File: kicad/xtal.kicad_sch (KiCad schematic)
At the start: 12 parts, among them Q1 NMOS, Q11 PMOS, Q12 NMOS, Q4 NMOS, Q6 PMOS, Y2 Crystal

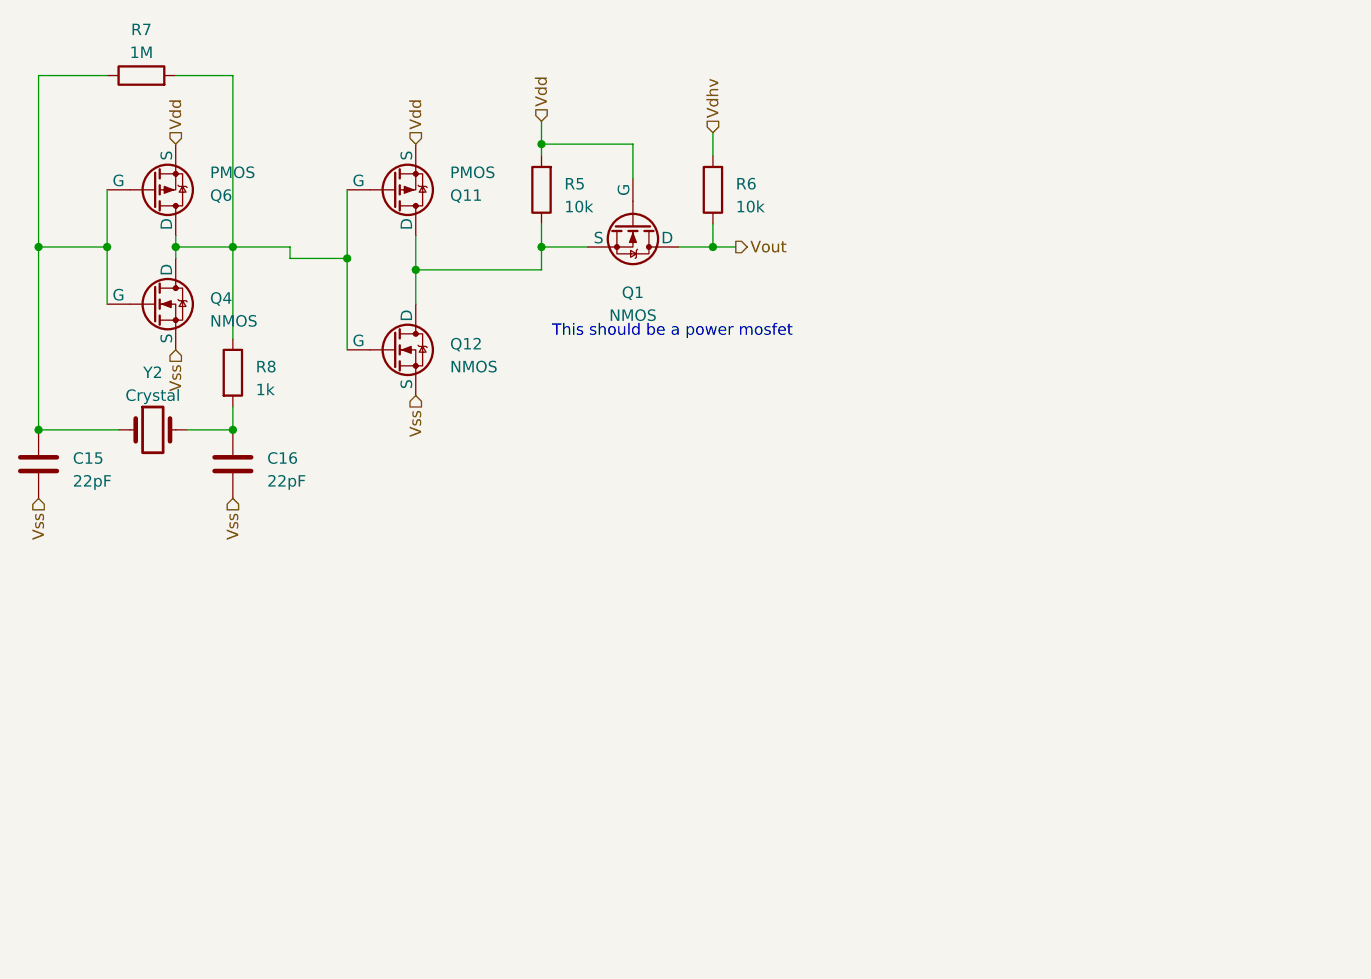
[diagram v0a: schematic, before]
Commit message: Add inverter driver
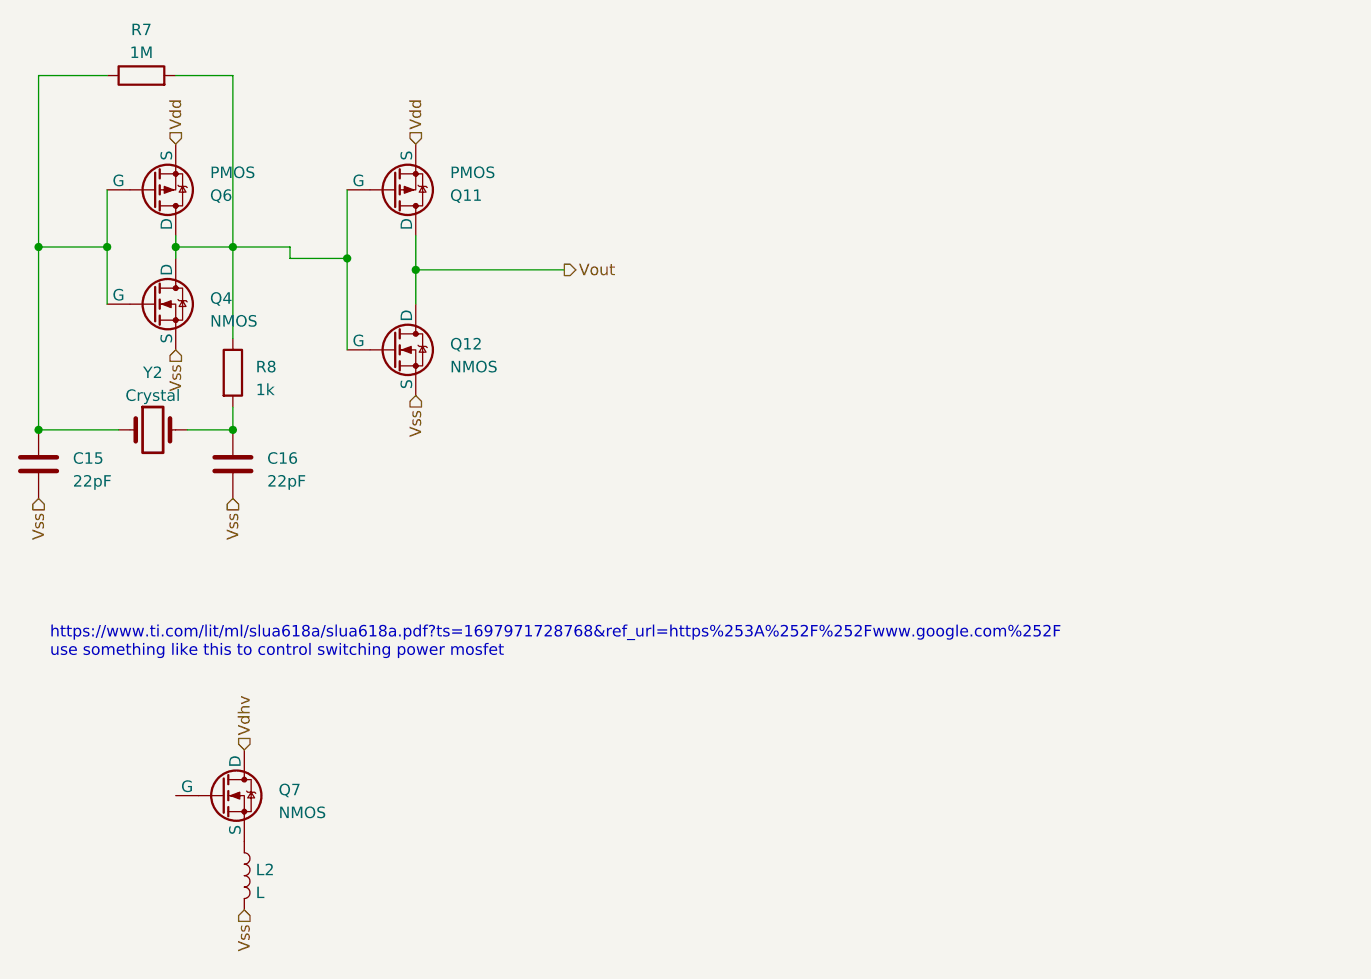
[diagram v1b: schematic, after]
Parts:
- removed Q1: NMOS, symbol Simulation_SPICE:NMOS
- removed R5, R6: 10k, symbol Device:R
- added L2: L, symbol Device:L
- added Q7: NMOS, symbol Simulation_SPICE:NMOS
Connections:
- net Vdhv: now also Q7.1 (D)
- net Vout: now also Q11.1 (D), Q12.1 (D)
- net Vss: now also L2.2
- new net: L2.1, Q7.3 (S)
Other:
- note added: "https://www.ti.com/lit/ml/slua618a/slua618a.pdf?ts=1697971728768&ref_url=https%253A%252F%252Fwww.google.com%252F use something like this to control switching power mosfet"
- note removed: "This should be a power mosfet"
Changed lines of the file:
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@@
   (junction (at 86.36 99.06) (diameter 0) (color 0 0 0 0)
   )
-  (junction (at 142.24 78.74) (diameter 0) (color 0 0 0 0)
-  )
   (junction (at 101.6 78.74) (diameter 0) (color 0 0 0 0)
   )
-  (junction (at 161.29 78.74) (diameter 0) (color 0 0 0 0)
-  )
   (junction (at 107.95 78.74) (diameter 0) (color 0 0 0 0)
   )
@@
   (junction (at 107.95 99.06) (diameter 0) (color 0 0 0 0)
   )
-  (junction (at 142.24 67.31) (diameter 0) (color 0 0 0 0)
-  )
   (junction (at 93.98 78.74) (diameter 0) (color 0 0 0 0)
   )
@@
     (stroke (width 0) (type default))
   )
-  (wire (pts (xy 161.29 66.04) (xy 161.29 68.58))
-    (stroke (width 0) (type default))
-  )
   (wire (pts (xy 93.98 78.74) (xy 93.98 85.09))
     (stroke (width 0) (type default))
@@
     (stroke (width 0) (type default))
   )
-  (wire (pts (xy 142.24 81.28) (xy 142.24 78.74))
-    (stroke (width 0) (type default))
-  )
-  (wire (pts (xy 128.27 81.28) (xy 142.24 81.28))
-    (stroke (width 0) (type default))
-  )
-  (wire (pts (xy 142.24 67.31) (xy 142.24 68.58))
-    (stroke (width 0) (type default))
-  )
   (wire (pts (xy 93.98 72.39) (xy 93.98 78.74))
     (stroke (width 0) (type default))
   )
-  (wire (pts (xy 161.29 78.74) (xy 163.83 78.74))
-    (stroke (width 0) (type default))
-  )
-  (wire (pts (xy 142.24 78.74) (xy 147.32 78.74))
+  (wire (pts (xy 128.27 81.28) (xy 144.78 81.28))
     (stroke (width 0) (type default))
   )
@@
     (stroke (width 0) (type default))
   )
-  (wire (pts (xy 152.4 71.12) (xy 152.4 67.31))
-    (stroke (width 0) (type default))
-  )
   (wire (pts (xy 120.65 80.01) (xy 120.65 90.17))
     (stroke (width 0) (type default))
@@
     (stroke (width 0) (type default))
   )
-  (wire (pts (xy 142.24 64.77) (xy 142.24 67.31))
-    (stroke (width 0) (type default))
-  )
   (wire (pts (xy 93.98 59.69) (xy 86.36 59.69))
     (stroke (width 0) (type default))
@@
     (stroke (width 0) (type default))
   )
-  (wire (pts (xy 152.4 67.31) (xy 142.24 67.31))
-    (stroke (width 0) (type default))
-  )
   (wire (pts (xy 107.95 88.9) (xy 107.95 78.74))
     (stroke (width 0) (type default))
   )
-  (wire (pts (xy 157.48 78.74) (xy 161.29 78.74))
-    (stroke (width 0) (type default))
-  )
   (wire (pts (xy 86.36 99.06) (xy 95.25 99.06))
     (stroke (width 0) (type default))
   )
-  (wire (pts (xy 142.24 76.2) (xy 142.24 78.74))
-    (stroke (width 0) (type default))
-  )
-  (wire (pts (xy 161.29 78.74) (xy 161.29 76.2))
-    (stroke (width 0) (type default))
-  )
   (wire (pts (xy 86.36 78.74) (xy 86.36 99.06))
     (stroke (width 0) (type default))
@@
     (stroke (width 0) (type default))
   )
-  (text "This should be a power mosfet" (at 170.18 88.9 0)
-    (effects (font (size 1.27 1.27)) (justify right bottom))
-  )
-  (hierarchical_label "Vdd" (shape input) (at 142.24 64.77 90) (fields_autoplaced)
-    (effects (font (size 1.27 1.27)) (justify left))
+  (text "https://www.ti.com/lit/ml/slua618a/slua618a.pdf?ts=1697971728768&ref_url=https%253A%252F%252Fwww.google.com%252F\nuse something like this to control switching power mosfet"
+    (at 87.63 124.46 0)
+    (effects (font (size 1.27 1.27)) (justify left bottom))
   )
   (hierarchical_label "Vss" (shape input) (at 107.95 106.68 270) (fields_autoplaced)
@@
     (effects (font (size 1.27 1.27)) (justify left))
   )
+  (hierarchical_label "Vss" (shape input) (at 109.22 152.4 270) (fields_autoplaced)
+    (effects (font (size 1.27 1.27)) (justify right))
+  )
   (hierarchical_label "Vss" (shape input) (at 128.27 95.25 270) (fields_autoplaced)
     (effects (font (size 1.27 1.27)) (justify right))
@@
     (effects (font (size 1.27 1.27)) (justify left))
   )
+  (hierarchical_label "Vdhv" (shape input) (at 109.22 134.62 90) (fields_autoplaced)
+    (effects (font (size 1.27 1.27)) (justify left))
+  )
   (hierarchical_label "Vss" (shape input) (at 101.6 90.17 270) (fields_autoplaced)
     (effects (font (size 1.27 1.27)) (justify right))
   )
-  (hierarchical_label "Vout" (shape output) (at 163.83 78.74 0) (fields_autoplaced)
-    (effects (font (size 1.27 1.27)) (justify left))
-  )
-  (hierarchical_label "Vdhv" (shape input) (at 161.29 66.04 90) (fields_autoplaced)
+  (hierarchical_label "Vout" (shape output) (at 144.78 81.28 0) (fields_autoplaced)
     (effects (font (size 1.27 1.27)) (justify left))
   )
@@
     )
   )
-  (symbol (lib_id "Device:R") (at 161.29 72.39 180) (unit 1)
-    (in_bom yes) (on_board yes) (dnp no) (fields_autoplaced)
-    (property "Reference" "R6" (at 163.83 71.755 0)
-      (effects (font (size 1.27 1.27)) (justify right))
-    )
-    (property "Value" "10k" (at 163.83 74.295 0)
-      (effects (font (size 1.27 1.27)) (justify right))
-    )
-    (property "Footprint" "" (at 163.068 72.39 90)
-      (effects (font (size 1.27 1.27)) hide)
-    )
-    (property "Datasheet" "~" (at 161.29 72.39 0)
-      (effects (font (size 1.27 1.27)) hide)
-    )
-    (pin "1")
-    (pin "2")
-    (instances
-      (project "kicad"
-        (path "/85f8f747-8376-4af6-9da4-afbb0f4bcd36/c5aef724-8676-4c81-889e-041c5ca81271/e305aaec-b373-422a-b2cb-386e797e1bef"
-          (reference "R6") (unit 1)
+  (symbol (lib_id "Device:L") (at 109.22 148.59 0) (unit 1)
+    (in_bom yes) (on_board yes) (dnp no) (fields_autoplaced)
+    (property "Reference" "L2" (at 110.49 147.955 0)
+      (effects (font (size 1.27 1.27)) (justify left))
+    )
+    (property "Value" "L" (at 110.49 150.495 0)
+      (effects (font (size 1.27 1.27)) (justify left))
+    )
+    (property "Footprint" "" (at 109.22 148.59 0)
+      (effects (font (size 1.27 1.27)) hide)
+    )
+    (property "Datasheet" "~" (at 109.22 148.59 0)
+      (effects (font (size 1.27 1.27)) hide)
+    )
+    (pin "1")
+    (pin "2")
+    (instances
+      (project "kicad"
+        (path "/85f8f747-8376-4af6-9da4-afbb0f4bcd36/c5aef724-8676-4c81-889e-041c5ca81271/e305aaec-b373-422a-b2cb-386e797e1bef"
+          (reference "L2") (unit 1)
         )
       )
@@
     )
   )
-  (symbol (lib_id "Simulation_SPICE:NMOS") (at 152.4 76.2 270) (unit 1)
-    (in_bom yes) (on_board yes) (dnp no) (fields_autoplaced)
-    (property "Reference" "Q1" (at 152.4 83.82 90)
-      (effects (font (size 1.27 1.27)))
-    )
-    (property "Value" "NMOS" (at 152.4 86.36 90)
-      (effects (font (size 1.27 1.27)))
-    )
-    (property "Footprint" "" (at 154.94 81.28 0)
-      (effects (font (size 1.27 1.27)) hide)
-    )
-    (property "Datasheet" "https://ngspice.sourceforge.io/docs/ngspice-manual.pdf" (at 139.7 76.2 0)
-      (effects (font (size 1.27 1.27)) hide)
-    )
-    (property "Sim.Device" "NMOS" (at 135.255 76.2 0)
-      (effects (font (size 1.27 1.27)) hide)
-    )
-    (property "Sim.Type" "VDMOS" (at 133.35 76.2 0)
-      (effects (font (size 1.27 1.27)) hide)
-    )
-    (property "Sim.Pins" "1=D 2=G 3=S" (at 137.16 76.2 0)
-      (effects (font (size 1.27 1.27)) hide)
-    )
-    (pin "1")
-    (pin "2")
-    (pin "3")
-    (instances
-      (project "kicad"
-        (path "/85f8f747-8376-4af6-9da4-afbb0f4bcd36/c5aef724-8676-4c81-889e-041c5ca81271/e305aaec-b373-422a-b2cb-386e797e1bef"
-          (reference "Q1") (unit 1)
-        )
-      )
-    )
-  )
   (symbol (lib_id "Device:Crystal") (at 99.06 99.06 0) (unit 1)
     (in_bom yes) (on_board yes) (dnp no) (fields_autoplaced)
@@
     )
   )
+  (symbol (lib_id "Simulation_SPICE:NMOS") (at 106.68 139.7 0) (unit 1)
+    (in_bom yes) (on_board yes) (dnp no) (fields_autoplaced)
+    (property "Reference" "Q7" (at 113.03 139.065 0)
+      (effects (font (size 1.27 1.27)) (justify left))
+    )
+    (property "Value" "NMOS" (at 113.03 141.605 0)
+      (effects (font (size 1.27 1.27)) (justify left))
+    )
+    (property "Footprint" "" (at 111.76 137.16 0)
+      (effects (font (size 1.27 1.27)) hide)
+    )
+    (property "Datasheet" "https://ngspice.sourceforge.io/docs/ngspice-manual.pdf" (at 106.68 152.4 0)
+      (effects (font (size 1.27 1.27)) hide)
+    )
+    (property "Sim.Device" "NMOS" (at 106.68 156.845 0)
+      (effects (font (size 1.27 1.27)) hide)
+    )
+    (property "Sim.Type" "VDMOS" (at 106.68 158.75 0)
+      (effects (font (size 1.27 1.27)) hide)
+    )
+    (property "Sim.Pins" "1=D 2=G 3=S" (at 106.68 154.94 0)
+      (effects (font (size 1.27 1.27)) hide)
+    )
+    (pin "1")
+    (pin "2")
+    (pin "3")
+    (instances
+      (project "kicad"
+        (path "/85f8f747-8376-4af6-9da4-afbb0f4bcd36/c5aef724-8676-4c81-889e-041c5ca81271/e305aaec-b373-422a-b2cb-386e797e1bef"
+          (reference "Q7") (unit 1)
+        )
+      )
+    )
+  )
   (symbol (lib_id "Simulation_SPICE:NMOS") (at 125.73 90.17 0) (unit 1)
     (in_bom yes) (on_board yes) (dnp no) (fields_autoplaced)
@@
         )
       )
-    )
-  )
-  (symbol (lib_id "Device:R") (at 142.24 72.39 180) (unit 1)
-    (in_bom yes) (on_board yes) (dnp no) (fields_autoplaced)
-    (property "Reference" "R5" (at 144.78 71.755 0)
-      (effects (font (size 1.27 1.27)) (justify right))
-    )
-    (property "Value" "10k" (at 144.78 74.295 0)
-      (effects (font (size 1.27 1.27)) (justify right))
-    )
-    (property "Footprint" "" (at 144.018 72.39 90)
-      (effects (font (size 1.27 1.27)) hide)
-    )
-    (property "Datasheet" "~" (at 142.24 72.39 0)
-      (effects (font (size 1.27 1.27)) hide)
-    )
-    (pin "1")
-    (pin "2")
-    (instances
-      (project "kicad"
-        (path "/85f8f747-8376-4af6-9da4-afbb0f4bcd36/c5aef724-8676-4c81-889e-041c5ca81271/e305aaec-b373-422a-b2cb-386e797e1bef"
-          (reference "R5") (unit 1)
-        )
-      )
